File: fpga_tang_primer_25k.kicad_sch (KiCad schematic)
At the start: 1 part, among them U1 Tang_Primer_25K_Module

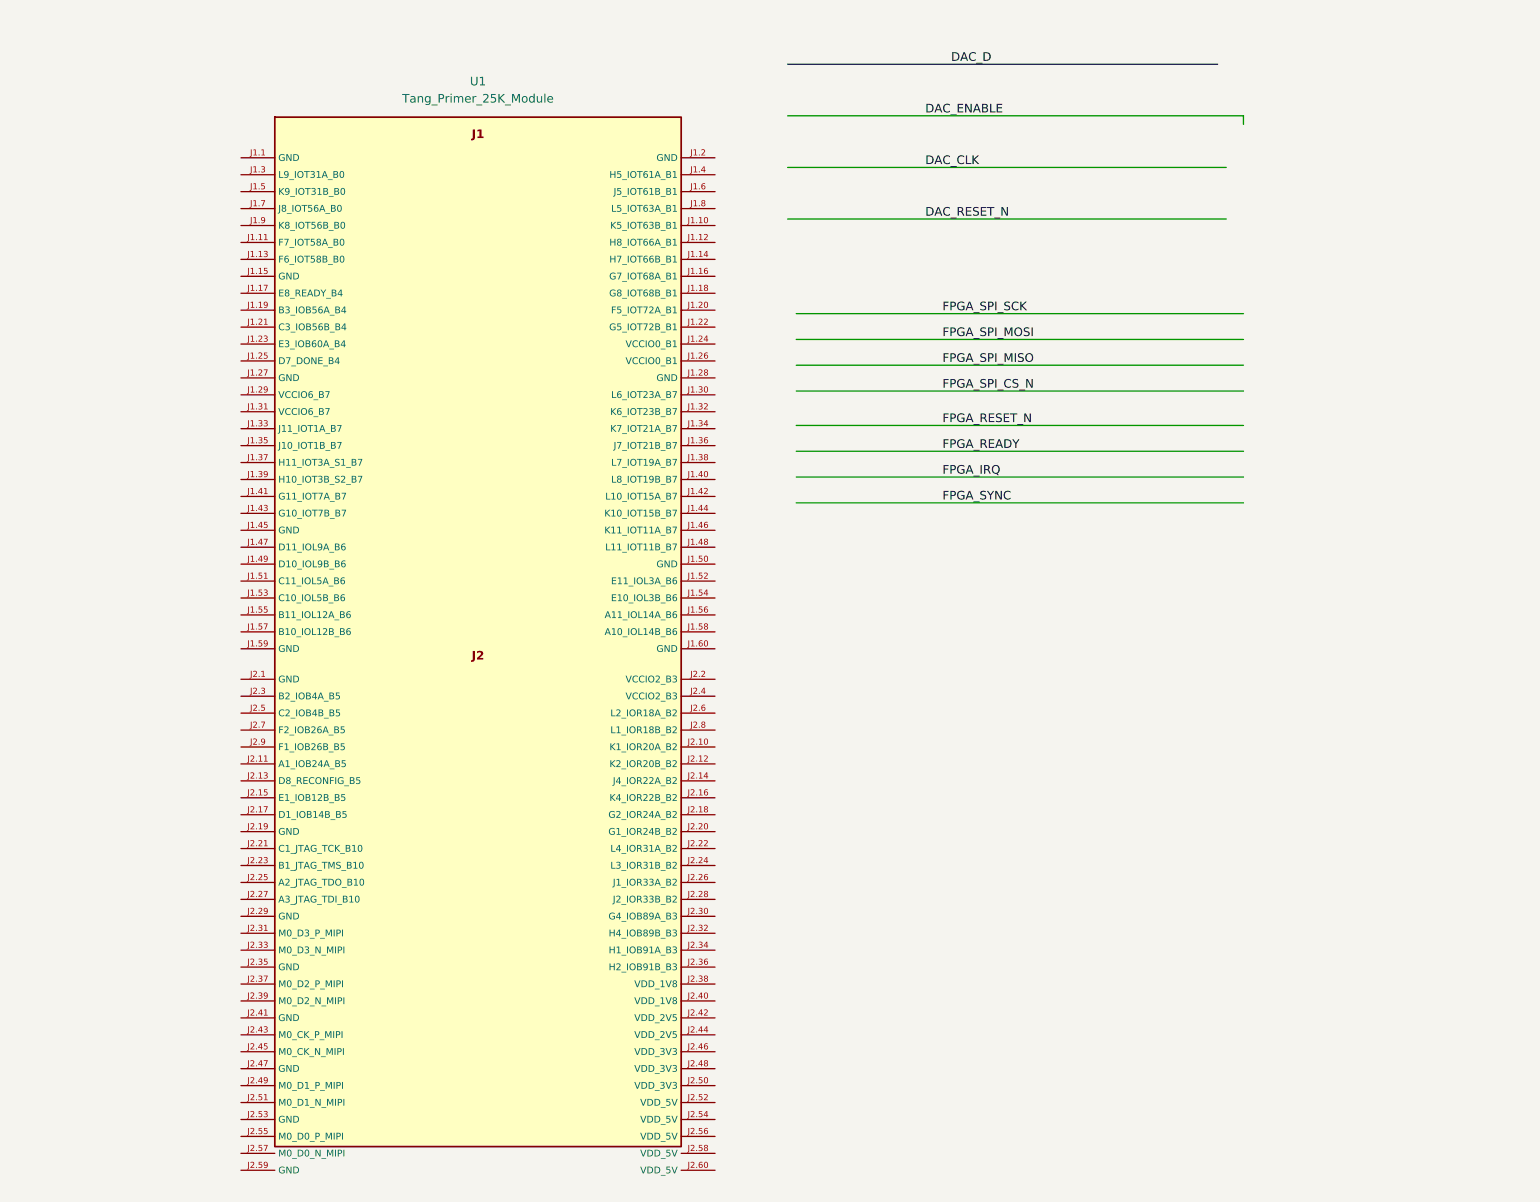
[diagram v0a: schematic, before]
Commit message: Fix fpga symbol and finish fpga pinout
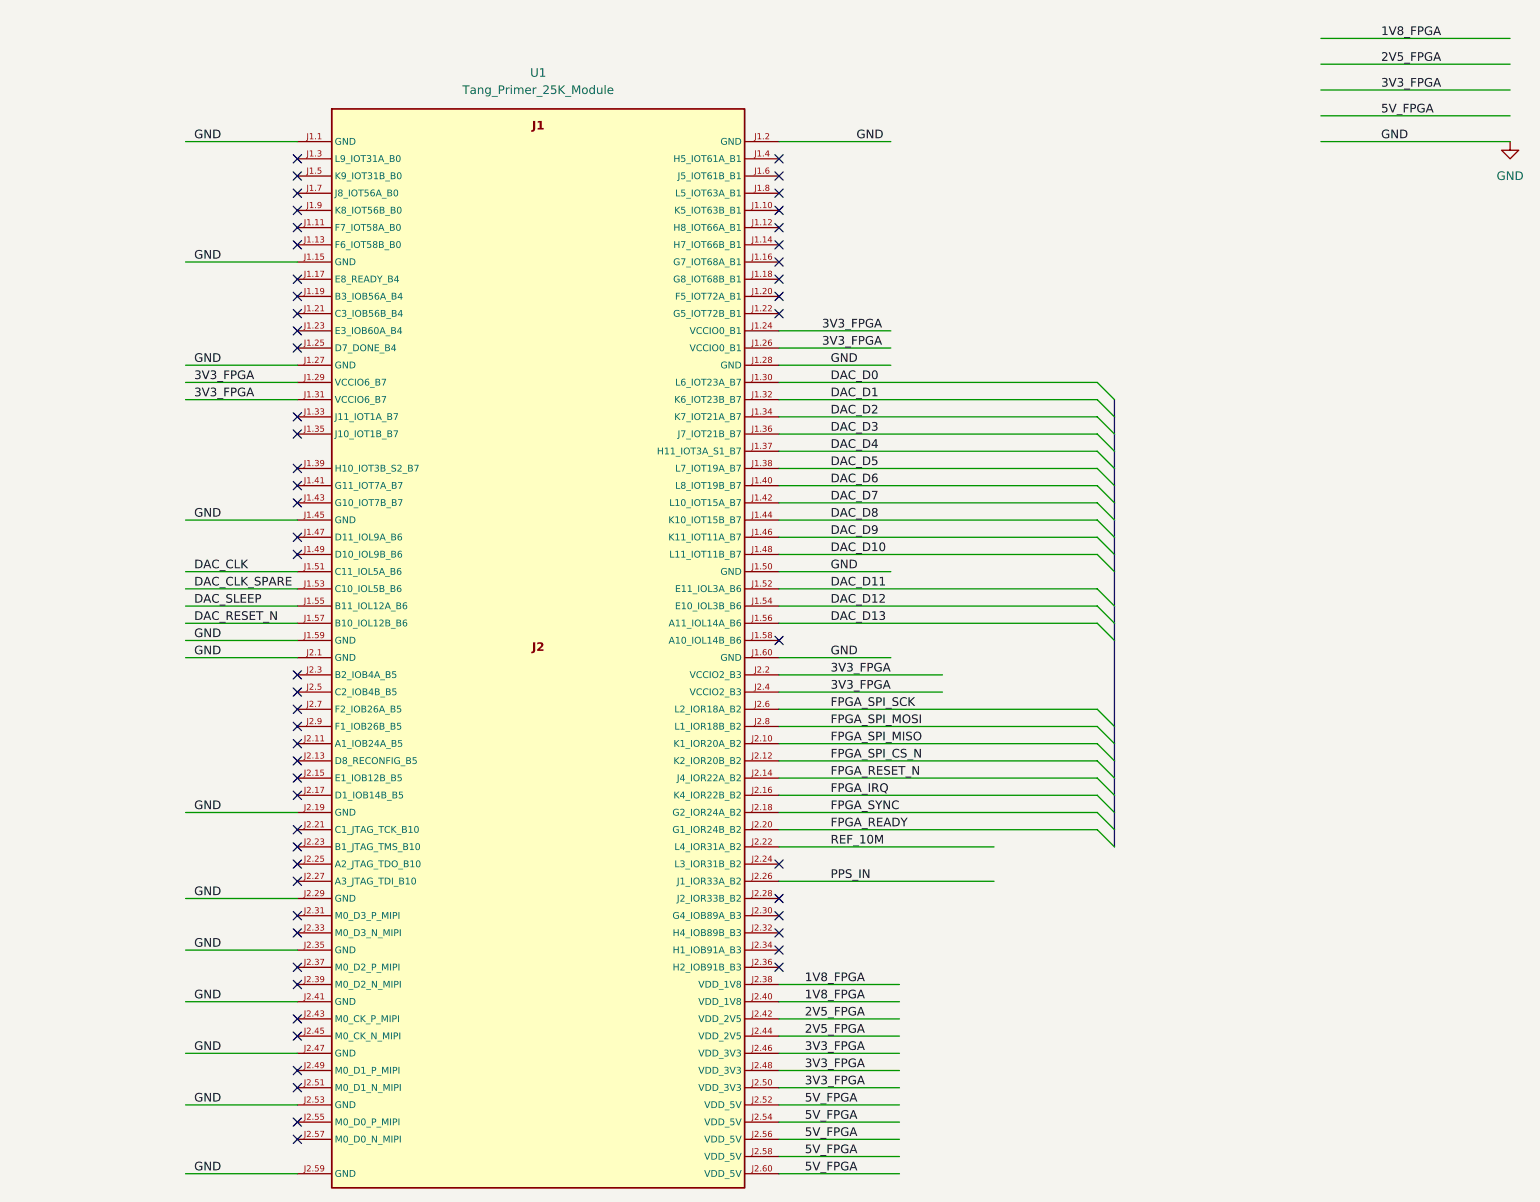
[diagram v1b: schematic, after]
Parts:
- removed U1: Tang_Primer_25K_Module, Tang_Primer_25K:Tang_Primer_25K_Module_2xDF40C-60DS, symbol Tang_Primer_25K:Tang_Primer_25K_Module
- added U1: Tang_Primer_25K_Module, Tang_Primer_25K:Tang_Primer_25K_Module_2xDF40C-60DS, symbol TangPrimer_25K:Tang_Primer_25K_Module
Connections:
- net DAC_CLK: now also U1.J1.51 (C11_IOL5A_B6)
- net DAC_RESET_N: now also U1.J1.57 (B10_IOL12B_B6)
- net FPGA_IRQ: now also U1.J2.16 (K4_IOR22B_B2)
- net FPGA_READY: now also U1.J2.20 (G1_IOR24B_B2)
- net FPGA_RESET_N: now also U1.J2.14 (J4_IOR22A_B2)
- net FPGA_SPI_CS_N: now also U1.J2.12 (K2_IOR20B_B2)
- net FPGA_SPI_MISO: now also U1.J2.10 (K1_IOR20A_B2)
- net FPGA_SPI_MOSI: now also U1.J2.8 (L1_IOR18B_B2)
- net FPGA_SPI_SCK: now also U1.J2.6 (L2_IOR18A_B2)
- net FPGA_SYNC: now also U1.J2.18 (G2_IOR24A_B2)
- new net 1V8_FPGA: U1.J2.38 (VDD_1V8), U1.J2.40 (VDD_1V8)
- new net 2V5_FPGA: U1.J2.42 (VDD_2V5), U1.J2.44 (VDD_2V5)
- new net 3V3_FPGA: U1.J1.24 (VCCIO0_B1), U1.J1.26 (VCCIO0_B1), U1.J1.29 (VCCIO6_B7), U1.J1.31 (VCCIO6_B7), U1.J2.2 (VCCIO2_B3), U1.J2.4 (VCCIO2_B3), U1.J2.46 (VDD_3V3), U1.J2.48 (VDD_3V3), U1.J2.50 (VDD_3V3)
- new net 5V_FPGA: U1.J2.52 (VDD_5V), U1.J2.54 (VDD_5V), U1.J2.56 (VDD_5V), U1.J2.58 (VDD_5V), U1.J2.60 (VDD_5V)
- new net DAC_CLK_SPARE: U1.J1.53 (C10_IOL5B_B6)
- new net DAC_D0: U1.J1.30 (L6_IOT23A_B7)
- new net DAC_D1: U1.J1.32 (K6_IOT23B_B7)
- new net DAC_D10: U1.J1.48 (L11_IOT11B_B7)
- new net DAC_D11: U1.J1.52 (E11_IOL3A_B6)
- new net DAC_D12: U1.J1.54 (E10_IOL3B_B6)
- new net DAC_D13: U1.J1.56 (A11_IOL14A_B6)
- new net DAC_D2: U1.J1.34 (K7_IOT21A_B7)
- new net DAC_D3: U1.J1.36 (J7_IOT21B_B7)
- new net DAC_D4: U1.J1.37 (H11_IOT3A_S1_B7)
- new net DAC_D5: U1.J1.38 (L7_IOT19A_B7)
- new net DAC_D6: U1.J1.40 (L8_IOT19B_B7)
- new net DAC_D7: U1.J1.42 (L10_IOT15A_B7)
- new net DAC_D8: U1.J1.44 (K10_IOT15B_B7)
- new net DAC_D9: U1.J1.46 (K11_IOT11A_B7)
- new net DAC_SLEEP: U1.J1.55 (B11_IOL12A_B6)
- new net GND: U1.J1.1 (GND), U1.J1.15 (GND), U1.J1.2 (GND), U1.J1.27 (GND), U1.J1.28 (GND), U1.J1.45 (GND), U1.J1.50 (GND), U1.J1.59 (GND), U1.J1.60 (GND), U1.J2.1 (GND), U1.J2.19 (GND), U1.J2.29 (GND), U1.J2.35 (GND), U1.J2.41 (GND), U1.J2.47 (GND), U1.J2.53 (GND), U1.J2.59 (GND)
- new net PPS_IN: U1.J2.26 (J1_IOR33A_B2)
- new net REF_10M: U1.J2.22 (L4_IOR31A_B2)
- no-connect marks 0 -> 57

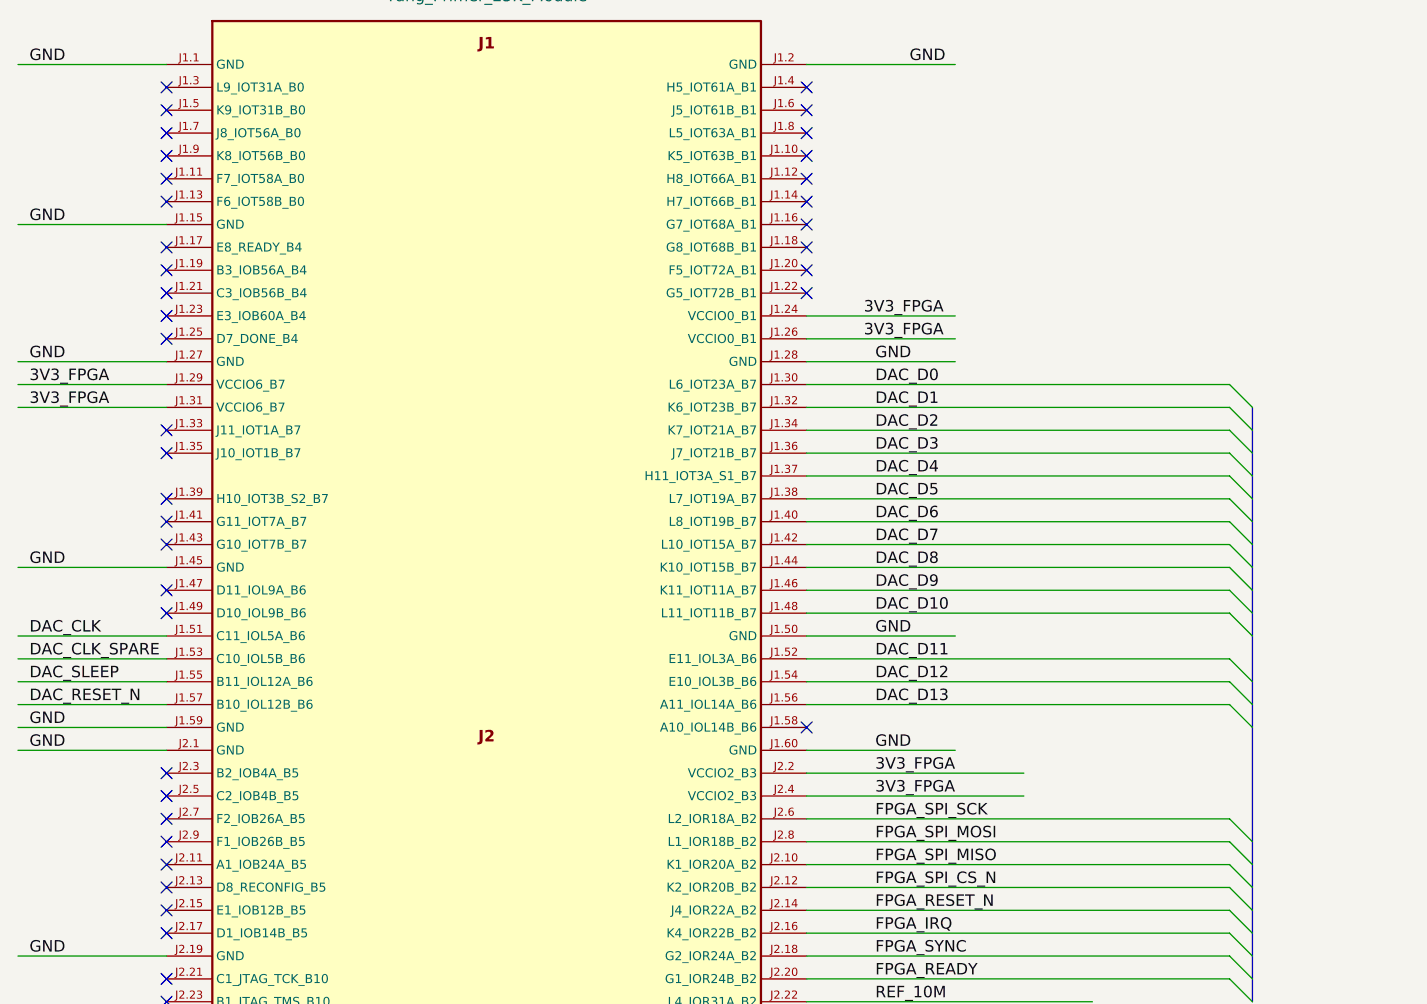
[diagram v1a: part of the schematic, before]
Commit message: Turn to new version Kicad
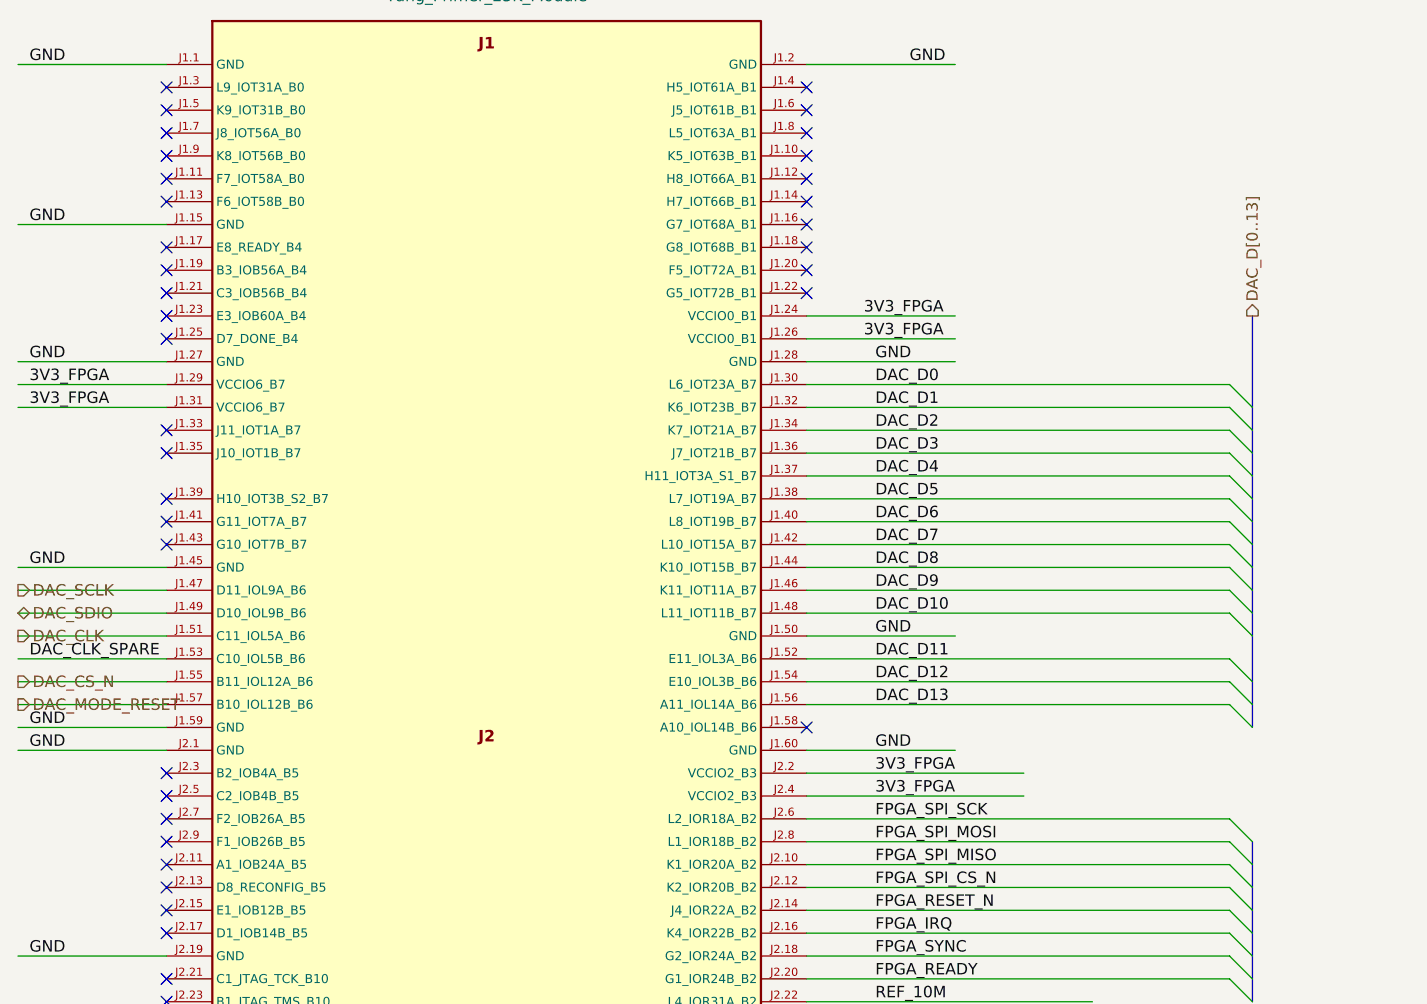
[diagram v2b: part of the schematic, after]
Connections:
- net DAC_SCLK: now reaches U1.J1.47 (D11_IOL9A_B6)
- net DAC_SDIO: now reaches U1.J1.49 (D10_IOL9B_B6)
- net DAC_RESET_N renamed DAC_MODE_RESET
- net DAC_SLEEP renamed DAC_CS_N
- no-connect marks 57 -> 55

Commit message: checkpoint: integrate GNSS RF and ADF4351 reference clock
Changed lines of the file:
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@@
+	(wire
+		(pts
+			(xy 16.51 17.78) (xy 26.67 17.78)
+		)
+		(stroke
+			(width 0)
+			(type default)
+		)
+	)
 	(wire
 		(pts
@@
 	(label "3V3_FPGA"
 		(at 137.16 113.03 0)
+		(effects
+			(font
+				(size 1.27 1.27)
+			)
+			(justify left bottom)
+		)
+	)
+	(label "REF_10M"
+		(at 16.51 17.78 0)
 		(effects
 			(font
@@
 		)
 	)
+	(hierarchical_label "REF_10M"
+		(shape input)
+		(at 26.67 17.78 0)
+		(effects
+			(font
+				(size 1.27 1.27)
+			)
+			(justify left)
+		)
+	)
